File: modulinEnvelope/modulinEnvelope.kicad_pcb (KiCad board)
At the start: 2 copper layers, 177.8 x 50.8 mm, 52 parts, among them J1 Conn_01x03_Socket, J2 Conn_01x03_Socket, Q1 BC548, Q2 BC548, Q3 BC548, Q4 BC548, Q5 BC548, Q6 BC548, Q7 2N7000, U1 TL074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

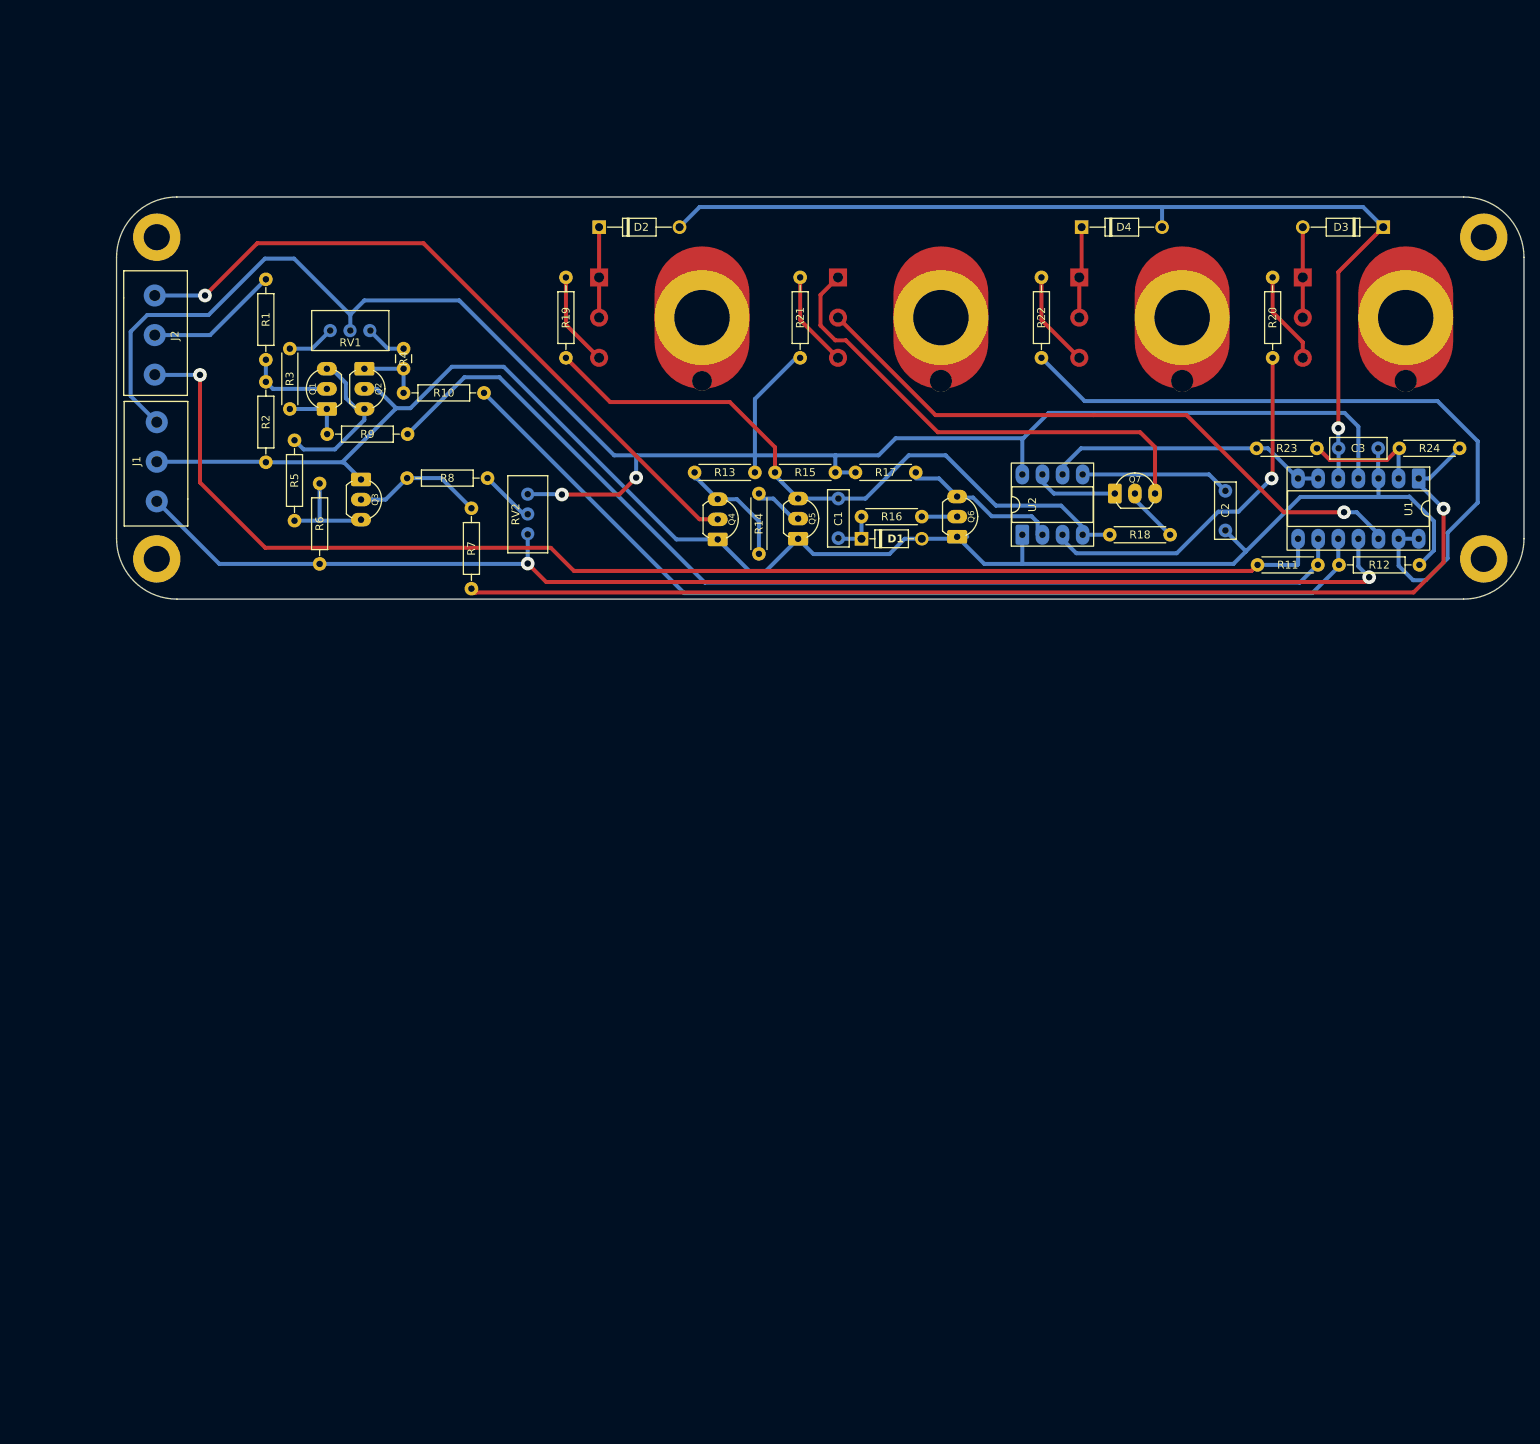
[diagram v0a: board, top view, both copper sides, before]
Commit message: Write out envelope circuit and make PCB, edit PSU
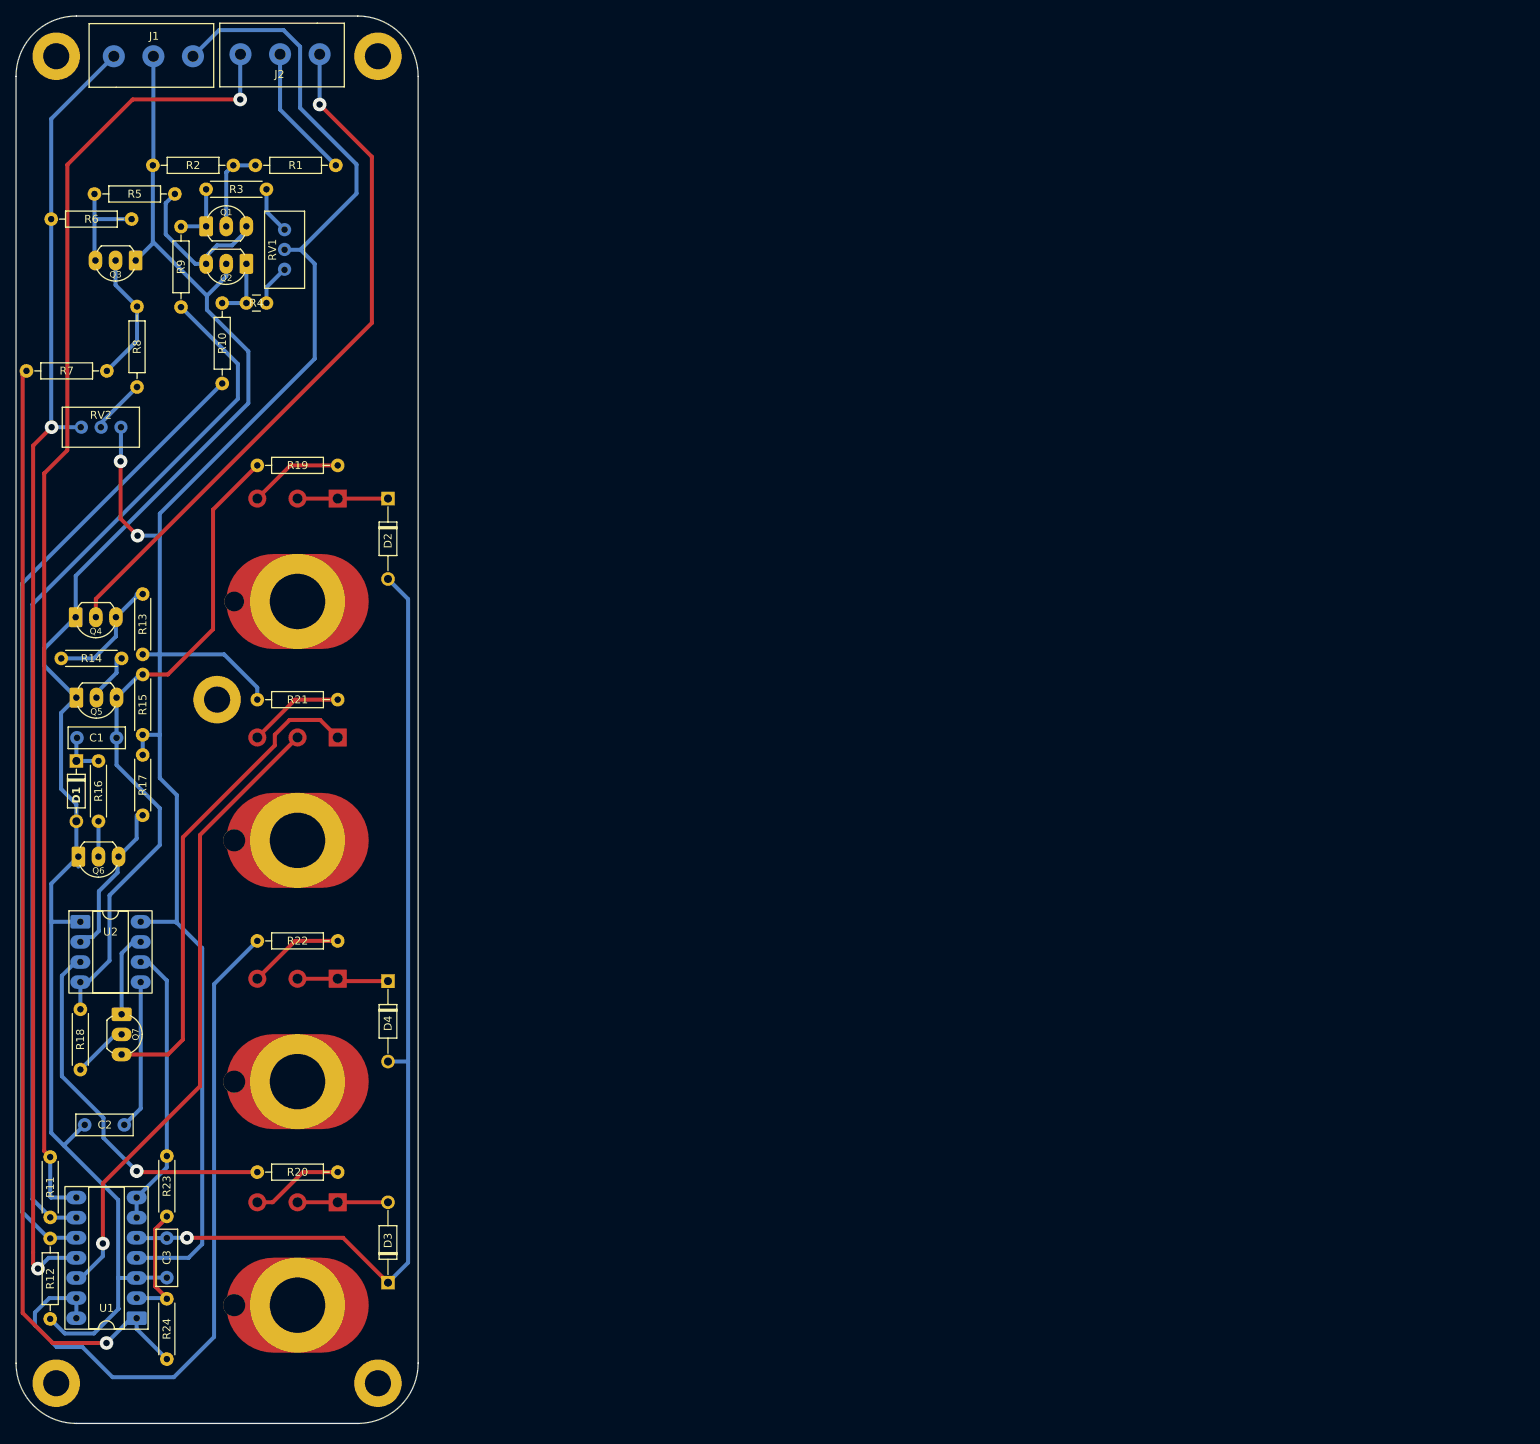
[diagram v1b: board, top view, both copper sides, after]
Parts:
- added REF**: MountingHole_M3_CNC, User:MountingHole_M3_CNC, F.Cu at (50.8, 101.6)
- moved REF** 208.2 mm to (30.5, 188.0), turned to -90 degrees
- moved REF** 201.2 mm to (71.1, 188.0), turned to -90 degrees
- moved R24 199.8 mm to (44.5, 184.9), turned to 90 degrees
- moved U1 193.6 mm to (40.6, 179.7), turned to 180 degrees
- moved RV4 187.5 mm to (61.0, 178.1), turned to 0 degrees
- moved C3 185.5 mm to (44.5, 174.6), turned to 90 degrees
- moved R12 183.7 mm to (29.7, 169.7), turned to -90 degrees
- moved D3 183.3 mm to (72.4, 175.3), turned to 90 degrees
- moved R23 174.7 mm to (44.5, 166.9), turned to 90 degrees
- moved R11 169.9 mm to (29.7, 159.4), turned to -90 degrees
- moved R20 163.5 mm to (66.0, 161.3), turned to 180 degrees
- moved C2 162.5 mm to (34.1, 155.3), turned to 0 degrees
- moved R18 153.4 mm to (33.5, 148.3), turned to 90 degrees
- moved RV6 147.7 mm to (61.0, 149.9), turned to 0 degrees
- moved Q7 145.1 mm to (38.7, 143.9), turned to -90 degrees
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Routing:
- net VCC: track 239.5 -> 240.1 mm
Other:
- board size 177.8 x 50.8 mm -> 50.8 x 177.8 mm

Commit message: Add VCF ciruit and edit for JLCPCB
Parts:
- removed J2: Conn_01x03_Socket, User:TerminalBlock_1x3_CNC
- J1: value Conn_01x03_Socket -> Screw_Terminal_01x06; footprint User:TerminalBlock_1x3_CNC -> User:TerminalBlock_1x6_CNC
- U2: footprint User:DIP8_CNC -> User:DIP-8_CNC
- moved J1 1.03 mm to (38.8, 20.1)
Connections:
- R1 pad 2: VCF_ENV -> IN
- R11 pad 1: ENV_VCA -> OUT
- U1 pad 8: ENV_VCA -> OUT
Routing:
- net OUT: track 0.00 -> 166.2 mm, vias 0 -> 1
- net ENV_VCA: track 166.2 -> 0.00 mm, vias 1 -> 0
- net VCF_ENV: track 17.1 -> 0.00 mm
- net IN: track 0.00 -> 17.1 mm
- net VEE: track 166.8 -> 167.9 mm
- net GND: track 217.3 -> 217.9 mm
- net VCC: track 240.1 -> 239.4 mm
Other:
- board text added: "Envelope"

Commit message: Add STEP files
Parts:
- moved REF** 173.0 mm to (71.1, 188.5), turned to 90 degrees
- moved REF** 173.0 mm to (30.5, 188.5), turned to 90 degrees
- moved REF** 172.0 mm to (30.5, 20.8), turned to 90 degrees
- moved REF** 172.0 mm to (71.1, 20.8), turned to 90 degrees
- moved J1 170.4 mm to (62.8, 188.7), turned to 180 degrees
- moved R24 161.5 mm to (57.1, 23.9), turned to -90 degrees
- moved U1 152.0 mm to (61.0, 29.1), turned to 0 degrees
- moved RV4 148.8 mm to (40.6, 30.7), turned to 180 degrees
- moved D3 148.2 mm to (29.2, 33.5), turned to -90 degrees
- moved R2 141.5 mm to (58.9, 174.7), turned to 180 degrees
- moved C3 141.0 mm to (57.1, 34.2), turned to -90 degrees
- moved R1 140.9 mm to (46.0, 174.7), turned to 180 degrees
- moved R12 137.2 mm to (71.9, 39.1), turned to 90 degrees
- moved R5 136.9 mm to (66.3, 171.1), turned to 180 degrees
- moved R3 134.6 mm to (52.2, 171.7), turned to 180 degrees
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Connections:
- RV5 pad 1: Net-(R21-Pad2) -> Net-(Q7-D)
- RV5 pad 3: Net-(Q7-D) -> Net-(R21-Pad2)
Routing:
- net Net-(Q7-D): track 61.5 -> 50.6 mm
- net Net-(R21-Pad2): track 12.1 -> 4.78 mm
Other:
- board text added: "GATE"
- board text added: "GND"
- board text added: "IN"
- board text added: "OUT"
- board text added: "VCC"
- board text added: "VEE"
